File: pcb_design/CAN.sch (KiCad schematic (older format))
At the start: 9 parts, among them Q2 2N7002PW, U2 ISO1050

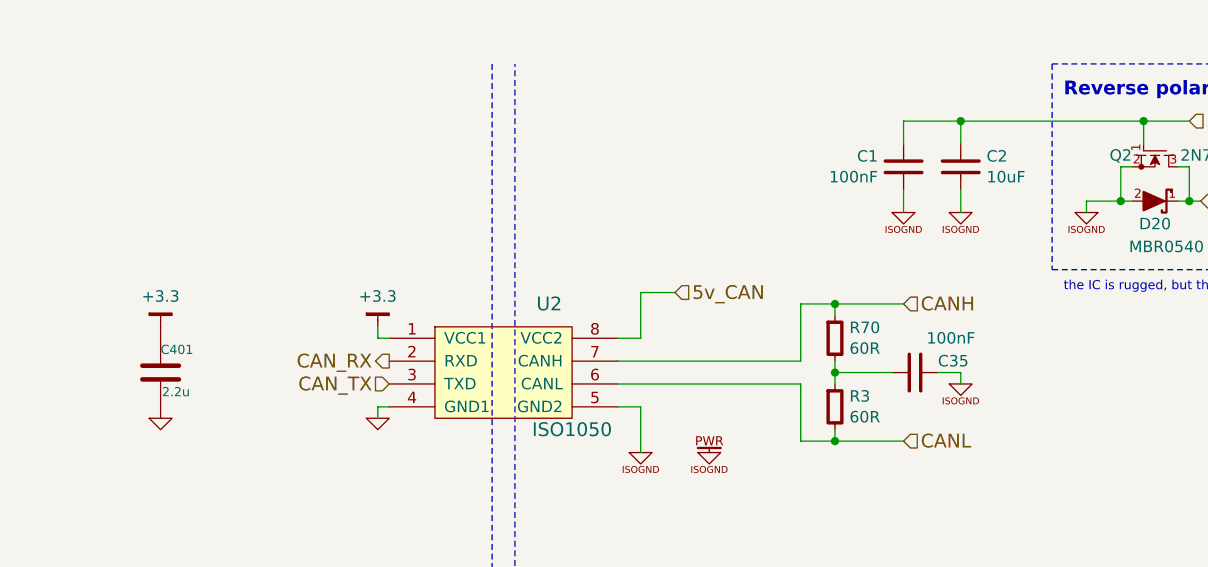
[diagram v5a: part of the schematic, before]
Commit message: Completed some part numbers
Signed-off-by: Marcos Chaparro <mchaparro@paltatech.com>
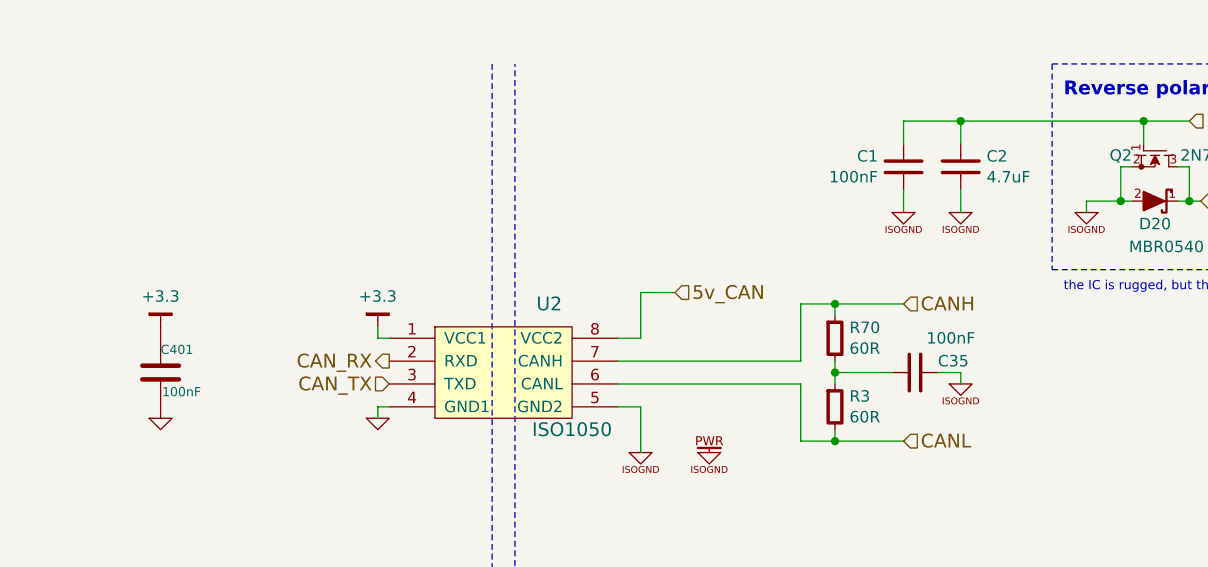
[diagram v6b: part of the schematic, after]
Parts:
- C1, C35: MFR (none) -> Murata Electronics North America; MPN (none) -> GRM188R71E104KA01D; SPN (none) -> 490-1524-1-ND; SPR (none) -> Digikey
- C2: value 10uF -> 4.7uF; MFR (none) -> Murata Electronics North America; MPN (none) -> GRM21BR71A475KA73K; SPN (none) -> 490-6479-1-ND; SPR (none) -> Digikey
- C401: value 2.2u -> 100nF; footprint CRF1:SMD-0603_c -> IPC7351-Nominal:CAPC1608X55; MFR (none) -> Murata Electronics North America; MPN (none) -> GRM188R71E104KA01D; SPN (none) -> 490-1524-1-ND; SPR (none) -> Digikey

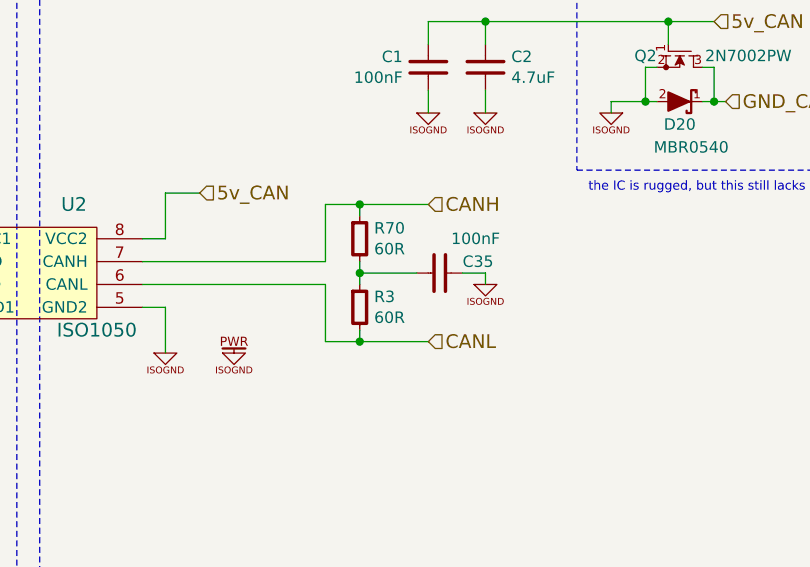
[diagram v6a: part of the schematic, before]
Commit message: Completed part number, manufacturer, etc fields. Simulated analog conditioning
Signed-off-by: Marcos Chaparro <mchaparro@paltatech.com>
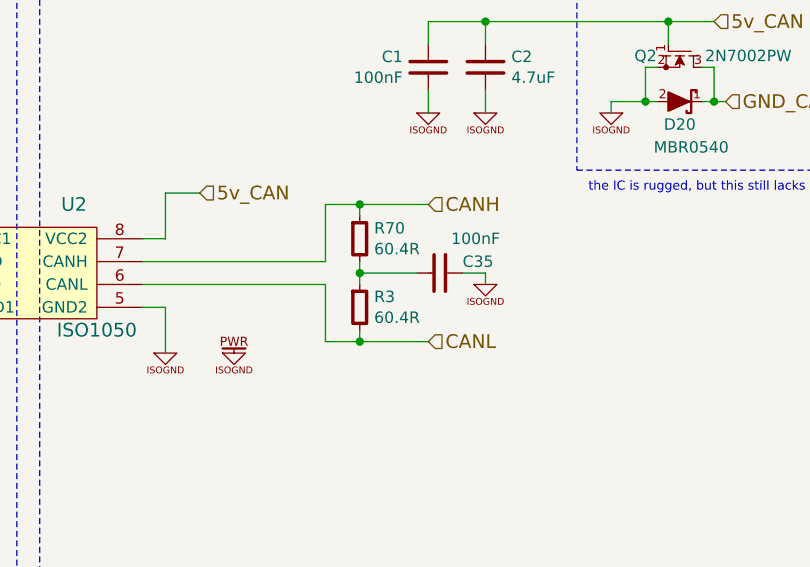
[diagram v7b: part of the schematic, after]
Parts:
- D20: MFR (none) -> Fairchild/ON Semiconductor; MPN (none) -> MBR0540; SPN (none) -> MBR0540CT-ND; SPR (none) -> Digikey
- Q2: MFR (none) -> Nexperia USA Inc.; MPN (none) -> 2N7002PW,115; SPN (none) -> 568-5987-1-ND; SPR (none) -> Digikey
- R3, R70: value 60R -> 60.4R; MFR (none) -> Yageo; MPN (none) -> RC0603FR-0760R4L; SPN (none) -> 311-60.4HRCT-ND; SPR (none) -> Digikey
- U2: MFR (none) -> Texas Instruments; MPN (none) -> ISO1050DUBR; SPN (none) -> 296-24818-1-ND; SPR (none) -> Digikey
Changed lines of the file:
@@
 F 1 "ISO1050" H 5800 3800 60 0000 C CNN
 F 2 "paltatech:SO8-ISO1050" H 5650 3850 60 0001 C CNN
-F 3 "" H 5650 3850 60 0000 C CNN
+F 3 "http://www.ti.com/lit/ds/symlink/iso1050.pdf" H 5650 3850 60 0001 C CNN
 F 4 "ISO1050DUBR" H 5600 3900 60 0001 C CNN "mfg#"
-F 5 "" H 0 0 50 0001 C CNN "MFR"
-F 6 "" H 0 0 50 0001 C CNN "MPN"
-F 7 "" H 0 0 50 0001 C CNN "SPR"
-F 8 "" H 0 0 50 0001 C CNN "SPN"
+F 5 "Texas Instruments" H 0 0 50 0001 C CNN "MFR"
+F 6 "ISO1050DUBR" H 0 0 50 0001 C CNN "MPN"
+F 7 "Digikey" H 0 0 50 0001 C CNN "SPR"
+F 8 "296-24818-1-ND" H 0 0 50 0001 C CNN "SPN"
 F 9 "" H 0 0 50 0001 C CNN "SPURL"
 	1    5500 4050
@@
 P 6950 4200
 F 0 "R3" H 7013 4246 50 0000 L CNN
-F 1 "60R" H 7013 4155 50 0000 L CNN
+F 1 "60.4R" H 7013 4155 50 0000 L CNN
 F 2 "IPC7351-Nominal:RESC1608X50" H 6950 4200 50 0001 C CNN
-F 3 "" H 6950 4250 60 0000 C CNN
+F 3 "" H 6950 4250 60 0001 C CNN
 F 4 "RES SMD 60 Ohm 1% [0603]" H 7700 4750 60 0001 C CNN "BOM"
-F 5 "" H 0 0 50 0001 C CNN "MFR"
-F 6 "" H 0 0 50 0001 C CNN "MPN"
-F 7 "" H 0 0 50 0001 C CNN "SPR"
-F 8 "" H 0 0 50 0001 C CNN "SPN"
+F 5 "Yageo" H 0 0 50 0001 C CNN "MFR"
+F 6 "RC0603FR-0760R4L" H 0 0 50 0001 C CNN "MPN"
+F 7 "Digikey" H 0 0 50 0001 C CNN "SPR"
+F 8 "311-60.4HRCT-ND" H 0 0 50 0001 C CNN "SPN"
 F 9 "" H 0 0 50 0001 C CNN "SPURL"
 	1    6950 4200
@@
 P 6950 3900
 F 0 "R70" H 7013 3946 50 0000 L CNN
-F 1 "60R" H 7013 3855 50 0000 L CNN
+F 1 "60.4R" H 7013 3855 50 0000 L CNN
 F 2 "IPC7351-Nominal:RESC1608X50" H 6950 3900 50 0001 C CNN
-F 3 "" H 6950 3950 60 0000 C CNN
+F 3 "" H 6950 3950 60 0001 C CNN
 F 4 "RES SMD 60 Ohm 1% [0603]" H 7700 4450 60 0001 C CNN "BOM"
-F 5 "" H 0 0 50 0001 C CNN "MFR"
-F 6 "" H 0 0 50 0001 C CNN "MPN"
-F 7 "" H 0 0 50 0001 C CNN "SPR"
-F 8 "" H 0 0 50 0001 C CNN "SPN"
+F 5 "Yageo" H 0 0 50 0001 C CNN "MFR"
+F 6 "RC0603FR-0760R4L" H 0 0 50 0001 C CNN "MPN"
+F 7 "Digikey" H 0 0 50 0001 C CNN "SPR"
+F 8 "311-60.4HRCT-ND" H 0 0 50 0001 C CNN "SPN"
 F 9 "" H 0 0 50 0001 C CNN "SPURL"
 	1    6950 3900
@@
 F 4 "2N7002PW,115" H 8350 3100 60 0001 C CNN "mfg#"
 F 5 "NMOS NXP 2N7002PW" H 50 -1100 60 0001 C CNN "BOM"
-F 6 "" H 0 0 50 0001 C CNN "MFR"
-F 7 "" H 0 0 50 0001 C CNN "MPN"
-F 8 "" H 0 0 50 0001 C CNN "SPR"
-F 9 "" H 0 0 50 0001 C CNN "SPN"
+F 6 "Nexperia USA Inc." H 0 0 50 0001 C CNN "MFR"
+F 7 "2N7002PW,115" H 0 0 50 0001 C CNN "MPN"
+F 8 "Digikey" H 0 0 50 0001 C CNN "SPR"
+F 9 "568-5987-1-ND" H 0 0 50 0001 C CNN "SPN"
 F 10 "" H 0 0 50 0001 C CNN "SPURL"
 	1    8350 3100
@@
 F 1 "MBR0540" V 8150 3250 50 0000 C CNN
 F 2 "smd-semi:SOD-123" H 200 -250 50 0001 C CNN
-F 3 "http://www.onsemi.com/pub_link/Collateral/MBR0540T1-D.PDF" H 200 -150 60 0001 C CNN
+F 3 "https://www.fairchildsemi.com/datasheets/MB/MBR0540.pdf" H 200 -150 60 0001 C CNN
 F 4 "SCHOTTKY MBR0540" H 200 -350 60 0001 C CNN "BOM"
-F 5 "" H 0 0 50 0001 C CNN "MFR"
-F 6 "" H 0 0 50 0001 C CNN "MPN"
-F 7 "" H 0 0 50 0001 C CNN "SPR"
-F 8 "" H 0 0 50 0001 C CNN "SPN"
+F 5 "Fairchild/ON Semiconductor" H 0 0 50 0001 C CNN "MFR"
+F 6 "MBR0540" H 0 0 50 0001 C CNN "MPN"
+F 7 "Digikey" H 0 0 50 0001 C CNN "SPR"
+F 8 "MBR0540CT-ND" H 0 0 50 0001 C CNN "SPN"
 F 9 "" H 0 0 50 0001 C CNN "SPURL"
 	1    8350 3300
